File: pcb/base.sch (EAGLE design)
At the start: 2 parts, among them IC1 27C64L

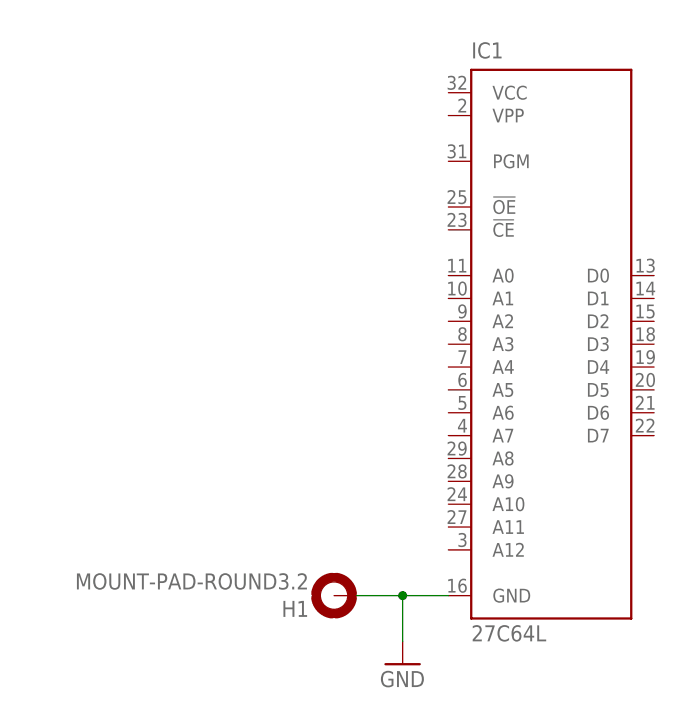
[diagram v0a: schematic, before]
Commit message: Changed mounting pad for the cufflink back.
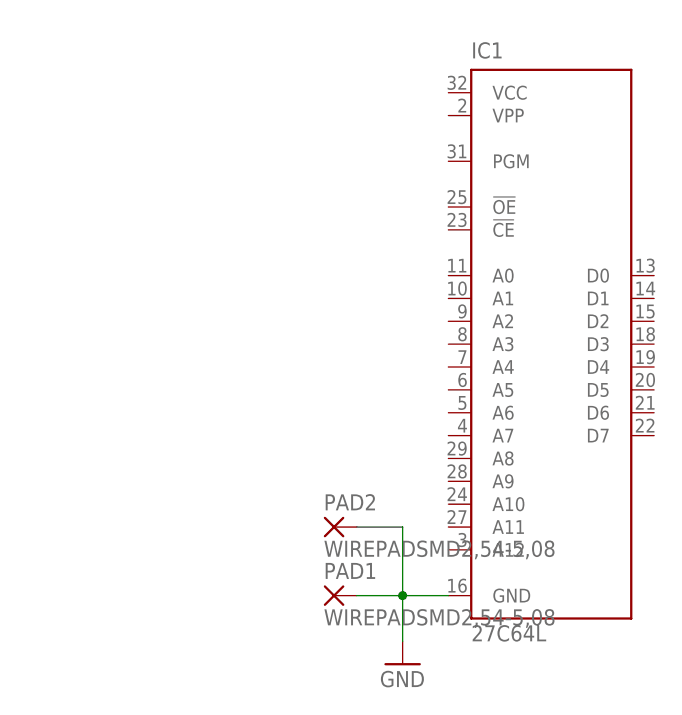
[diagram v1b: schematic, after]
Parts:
- removed H1: MOUNT-PAD-ROUND3.2, holes:MOUNT-PAD-ROUND3.2
- added PAD1, PAD2: WIREPADSMD2,54-5,08, wirepad:WIREPADSMD2,54-5,08
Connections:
- net GND: now also PAD1.P, PAD2.P; no longer H1.MOUNT
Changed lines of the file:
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@@
 <grid distance="0.1" unitdist="inch" unit="inch" style="lines" multiple="1" display="no" altdistance="0.01" altunitdist="inch" altunit="inch"/>
 <layers>
-<layer number="1" name="Top" color="4" fill="1" visible="no" active="no"/>
-<layer number="16" name="Bottom" color="1" fill="1" visible="no" active="no"/>
-<layer number="17" name="Pads" color="2" fill="1" visible="no" active="no"/>
-<layer number="18" name="Vias" color="2" fill="1" visible="no" active="no"/>
-<layer number="19" name="Unrouted" color="6" fill="1" visible="no" active="no"/>
-<layer number="20" name="Dimension" color="15" fill="1" visible="no" active="no"/>
-<layer number="21" name="tPlace" color="7" fill="1" visible="no" active="no"/>
-<layer number="22" name="bPlace" color="7" fill="1" visible="no" active="no"/>
-<layer number="23" name="tOrigins" color="15" fill="1" visible="no" active="no"/>
-<layer number="24" name="bOrigins" color="15" fill="1" visible="no" active="no"/>
-<layer number="25" name="tNames" color="7" fill="1" visible="no" active="no"/>
-<layer number="26" name="bNames" color="7" fill="1" visible="no" active="no"/>
-<layer number="27" name="tValues" color="7" fill="1" visible="no" active="no"/>
-<layer number="28" name="bValues" color="7" fill="1" visible="no" active="no"/>
+<layer number="1" name="Top" color="4" fill="1" visible="yes" active="no"/>
+<layer number="16" name="Bottom" color="1" fill="1" visible="yes" active="no"/>
+<layer number="17" name="Pads" color="2" fill="1" visible="yes" active="no"/>
+<layer number="18" name="Vias" color="2" fill="1" visible="yes" active="no"/>
+<layer number="19" name="Unrouted" color="6" fill="1" visible="yes" active="no"/>
+<layer number="20" name="Dimension" color="15" fill="1" visible="yes" active="no"/>
+<layer number="21" name="tPlace" color="7" fill="1" visible="yes" active="no"/>
+<layer number="22" name="bPlace" color="7" fill="1" visible="yes" active="no"/>
+<layer number="23" name="tOrigins" color="15" fill="1" visible="yes" active="no"/>
+<layer number="24" name="bOrigins" color="15" fill="1" visible="yes" active="no"/>
+<layer number="25" name="tNames" color="7" fill="1" visible="yes" active="no"/>
+<layer number="26" name="bNames" color="7" fill="1" visible="yes" active="no"/>
+<layer number="27" name="tValues" color="7" fill="1" visible="yes" active="no"/>
+<layer number="28" name="bValues" color="7" fill="1" visible="yes" active="no"/>
 <layer number="29" name="tStop" color="7" fill="3" visible="no" active="no"/>
 <layer number="30" name="bStop" color="7" fill="6" visible="no" active="no"/>
@@
 <layer number="35" name="tGlue" color="7" fill="4" visible="no" active="no"/>
 <layer number="36" name="bGlue" color="7" fill="5" visible="no" active="no"/>
-<layer number="37" name="tTest" color="7" fill="1" visible="no" active="no"/>
-<layer number="38" name="bTest" color="7" fill="1" visible="no" active="no"/>
+<layer number="37" name="tTest" color="7" fill="1" visible="yes" active="no"/>
+<layer number="38" name="bTest" color="7" fill="1" visible="yes" active="no"/>
 <layer number="39" name="tKeepout" color="4" fill="11" visible="no" active="no"/>
 <layer number="40" name="bKeepout" color="1" fill="11" visible="no" active="no"/>
@@
 <layer number="44" name="Drills" color="7" fill="1" visible="no" active="no"/>
 <layer number="45" name="Holes" color="7" fill="1" visible="no" active="no"/>
-<layer number="46" name="Milling" color="3" fill="1" visible="no" active="no"/>
-<layer number="47" name="Measures" color="7" fill="1" visible="no" active="no"/>
-<layer number="48" name="Document" color="7" fill="1" visible="no" active="no"/>
-<layer number="49" name="Reference" color="7" fill="1" visible="no" active="no"/>
-<layer number="51" name="tDocu" color="6" fill="1" visible="no" active="no"/>
-<layer number="52" name="bDocu" color="7" fill="1" visible="no" active="no"/>
+<layer number="46" name="Milling" color="3" fill="1" visible="yes" active="no"/>
+<layer number="47" name="Measures" color="7" fill="1" visible="yes" active="no"/>
+<layer number="48" name="Document" color="7" fill="1" visible="yes" active="no"/>
+<layer number="49" name="Reference" color="7" fill="1" visible="yes" active="no"/>
+<layer number="51" name="tDocu" color="7" fill="1" visible="yes" active="no"/>
+<layer number="52" name="bDocu" color="7" fill="1" visible="yes" active="no"/>
 <layer number="90" name="Modules" color="5" fill="1" visible="yes" active="yes"/>
 <layer number="91" name="Nets" color="2" fill="1" visible="yes" active="yes"/>
@@
 <parts>
 <part name="IC1" library="microchip" deviceset="27*64" device="L" technology="C"/>
-<part name="H1" library="holes" deviceset="MOUNT-PAD-ROUND" device="3.2"/>
 <part name="GND1" library="supply1" deviceset="GND" device=""/>
+<part name="PAD1" library="wirepad" deviceset="WIREPAD" device="SMD2,54-5,08" value="WIREPADSMD2,54-5,08"/>
+<part name="PAD2" library="wirepad" deviceset="WIREPAD" device="SMD2,54-5,08" value="WIREPADSMD2,54-5,08"/>
 </parts>
 <sheets>
@@
 <instances>
 <instance part="IC1" gate="G$1" x="15.24" y="38.1"/>
-<instance part="H1" gate="G$1" x="-7.62" y="10.16" rot="R180"/>
 <instance part="GND1" gate="1" x="0" y="2.54"/>
+<instance part="PAD1" gate="G$1" x="-7.62" y="10.16"/>
+<instance part="PAD2" gate="G$1" x="-7.62" y="17.78"/>
 </instances>
 <busses>
@@
 <pinref part="IC1" gate="G$1" pin="GND"/>
 <wire x1="0" y1="10.16" x2="5.08" y2="10.16" width="0.1524" layer="91"/>
-<pinref part="H1" gate="G$1" pin="MOUNT"/>
-<wire x1="0" y1="10.16" x2="-5.08" y2="10.16" width="0.1524" layer="91"/>
+<pinref part="PAD1" gate="G$1" pin="P"/>
+<wire x1="-5.08" y1="10.16" x2="0" y2="10.16" width="0.1524" layer="91"/>
+<wire x1="0" y1="10.16" x2="0" y2="17.78" width="0.1524" layer="91"/>
+<pinref part="PAD2" gate="G$1" pin="P"/>
+<wire x1="0" y1="17.78" x2="-5.08" y2="17.78" width="0.1524" layer="91"/>
 <junction x="0" y="10.16"/>
 </segment>

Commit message: Connected the rest of the pins.
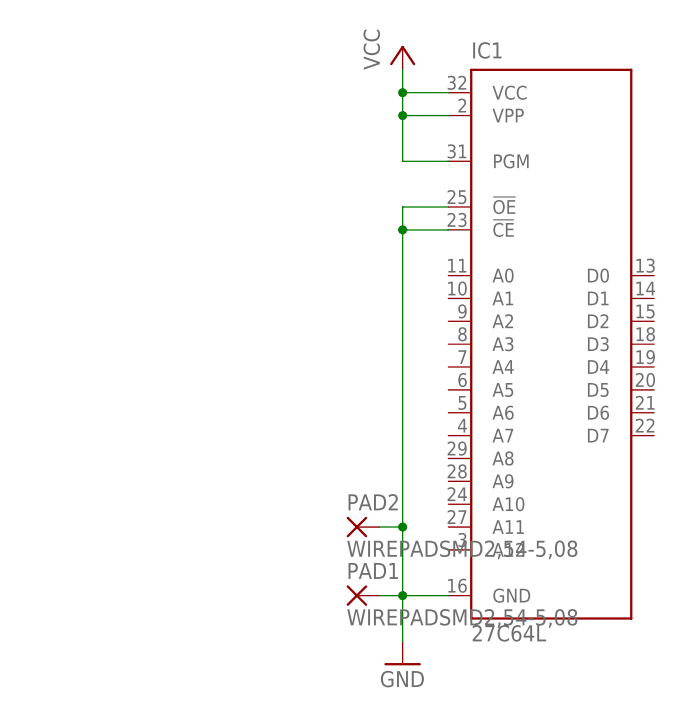
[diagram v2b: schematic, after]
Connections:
- new net VCC: IC1.PGM, IC1.VCC, IC1.VPP
- net GND: now also IC1.!CE, IC1.!OE
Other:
- moved on the sheet: PAD1, PAD2
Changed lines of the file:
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@@
 <grid distance="0.1" unitdist="inch" unit="inch" style="lines" multiple="1" display="no" altdistance="0.01" altunitdist="inch" altunit="inch"/>
 <layers>
-<layer number="1" name="Top" color="4" fill="1" visible="yes" active="no"/>
-<layer number="16" name="Bottom" color="1" fill="1" visible="yes" active="no"/>
-<layer number="17" name="Pads" color="2" fill="1" visible="yes" active="no"/>
-<layer number="18" name="Vias" color="2" fill="1" visible="yes" active="no"/>
-<layer number="19" name="Unrouted" color="6" fill="1" visible="yes" active="no"/>
-<layer number="20" name="Dimension" color="15" fill="1" visible="yes" active="no"/>
-<layer number="21" name="tPlace" color="7" fill="1" visible="yes" active="no"/>
-<layer number="22" name="bPlace" color="7" fill="1" visible="yes" active="no"/>
-<layer number="23" name="tOrigins" color="15" fill="1" visible="yes" active="no"/>
-<layer number="24" name="bOrigins" color="15" fill="1" visible="yes" active="no"/>
-<layer number="25" name="tNames" color="7" fill="1" visible="yes" active="no"/>
-<layer number="26" name="bNames" color="7" fill="1" visible="yes" active="no"/>
-<layer number="27" name="tValues" color="7" fill="1" visible="yes" active="no"/>
-<layer number="28" name="bValues" color="7" fill="1" visible="yes" active="no"/>
+<layer number="1" name="Top" color="4" fill="1" visible="no" active="no"/>
+<layer number="16" name="Bottom" color="1" fill="1" visible="no" active="no"/>
+<layer number="17" name="Pads" color="2" fill="1" visible="no" active="no"/>
+<layer number="18" name="Vias" color="2" fill="1" visible="no" active="no"/>
+<layer number="19" name="Unrouted" color="6" fill="1" visible="no" active="no"/>
+<layer number="20" name="Dimension" color="15" fill="1" visible="no" active="no"/>
+<layer number="21" name="tPlace" color="7" fill="1" visible="no" active="no"/>
+<layer number="22" name="bPlace" color="7" fill="1" visible="no" active="no"/>
+<layer number="23" name="tOrigins" color="15" fill="1" visible="no" active="no"/>
+<layer number="24" name="bOrigins" color="15" fill="1" visible="no" active="no"/>
+<layer number="25" name="tNames" color="7" fill="1" visible="no" active="no"/>
+<layer number="26" name="bNames" color="7" fill="1" visible="no" active="no"/>
+<layer number="27" name="tValues" color="7" fill="1" visible="no" active="no"/>
+<layer number="28" name="bValues" color="7" fill="1" visible="no" active="no"/>
 <layer number="29" name="tStop" color="7" fill="3" visible="no" active="no"/>
 <layer number="30" name="bStop" color="7" fill="6" visible="no" active="no"/>
@@
 <layer number="35" name="tGlue" color="7" fill="4" visible="no" active="no"/>
 <layer number="36" name="bGlue" color="7" fill="5" visible="no" active="no"/>
-<layer number="37" name="tTest" color="7" fill="1" visible="yes" active="no"/>
-<layer number="38" name="bTest" color="7" fill="1" visible="yes" active="no"/>
+<layer number="37" name="tTest" color="7" fill="1" visible="no" active="no"/>
+<layer number="38" name="bTest" color="7" fill="1" visible="no" active="no"/>
 <layer number="39" name="tKeepout" color="4" fill="11" visible="no" active="no"/>
 <layer number="40" name="bKeepout" color="1" fill="11" visible="no" active="no"/>
@@
 <layer number="44" name="Drills" color="7" fill="1" visible="no" active="no"/>
 <layer number="45" name="Holes" color="7" fill="1" visible="no" active="no"/>
-<layer number="46" name="Milling" color="3" fill="1" visible="yes" active="no"/>
-<layer number="47" name="Measures" color="7" fill="1" visible="yes" active="no"/>
-<layer number="48" name="Document" color="7" fill="1" visible="yes" active="no"/>
-<layer number="49" name="Reference" color="7" fill="1" visible="yes" active="no"/>
-<layer number="51" name="tDocu" color="7" fill="1" visible="yes" active="no"/>
-<layer number="52" name="bDocu" color="7" fill="1" visible="yes" active="no"/>
+<layer number="46" name="Milling" color="3" fill="1" visible="no" active="no"/>
+<layer number="47" name="Measures" color="7" fill="1" visible="no" active="no"/>
+<layer number="48" name="Document" color="7" fill="1" visible="no" active="no"/>
+<layer number="49" name="Reference" color="7" fill="1" visible="no" active="no"/>
+<layer number="51" name="tDocu" color="7" fill="1" visible="no" active="no"/>
+<layer number="52" name="bDocu" color="7" fill="1" visible="no" active="no"/>
 <layer number="90" name="Modules" color="5" fill="1" visible="yes" active="yes"/>
 <layer number="91" name="Nets" color="2" fill="1" visible="yes" active="yes"/>
@@
 <part name="PAD1" library="wirepad" deviceset="WIREPAD" device="SMD2,54-5,08" value="WIREPADSMD2,54-5,08"/>
 <part name="PAD2" library="wirepad" deviceset="WIREPAD" device="SMD2,54-5,08" value="WIREPADSMD2,54-5,08"/>
+<part name="P+1" library="supply1" deviceset="VCC" device=""/>
 </parts>
 <sheets>
@@
 <instance part="IC1" gate="G$1" x="15.24" y="38.1"/>
 <instance part="GND1" gate="1" x="0" y="2.54"/>
-<instance part="PAD1" gate="G$1" x="-7.62" y="10.16"/>
-<instance part="PAD2" gate="G$1" x="-7.62" y="17.78"/>
+<instance part="PAD1" gate="G$1" x="-5.08" y="10.16"/>
+<instance part="PAD2" gate="G$1" x="-5.08" y="17.78"/>
+<instance part="P+1" gate="VCC" x="0" y="71.12"/>
 </instances>
 <busses>
@@
 <wire x1="0" y1="10.16" x2="5.08" y2="10.16" width="0.1524" layer="91"/>
 <pinref part="PAD1" gate="G$1" pin="P"/>
-<wire x1="-5.08" y1="10.16" x2="0" y2="10.16" width="0.1524" layer="91"/>
+<wire x1="-2.54" y1="10.16" x2="0" y2="10.16" width="0.1524" layer="91"/>
 <wire x1="0" y1="10.16" x2="0" y2="17.78" width="0.1524" layer="91"/>
 <pinref part="PAD2" gate="G$1" pin="P"/>
-<wire x1="0" y1="17.78" x2="-5.08" y2="17.78" width="0.1524" layer="91"/>
+<wire x1="0" y1="17.78" x2="-2.54" y2="17.78" width="0.1524" layer="91"/>
 <junction x="0" y="10.16"/>
+<pinref part="IC1" gate="G$1" pin="!OE"/>
+<wire x1="0" y1="53.34" x2="0" y2="50.8" width="0.1524" layer="91"/>
+<wire x1="0" y1="50.8" x2="0" y2="17.78" width="0.1524" layer="91"/>
+<wire x1="5.08" y1="53.34" x2="0" y2="53.34" width="0.1524" layer="91"/>
+<pinref part="IC1" gate="G$1" pin="!CE"/>
+<wire x1="5.08" y1="50.8" x2="0" y2="50.8" width="0.1524" layer="91"/>
+<junction x="0" y="50.8"/>
+<junction x="0" y="17.78"/>
+</segment>
+</net>
+<net name="VCC" class="0">
+<segment>
+<pinref part="IC1" gate="G$1" pin="VCC"/>
+<pinref part="P+1" gate="VCC" pin="VCC"/>
+<wire x1="5.08" y1="66.04" x2="0" y2="66.04" width="0.1524" layer="91"/>
+<wire x1="0" y1="66.04" x2="0" y2="68.58" width="0.1524" layer="91"/>
+<pinref part="IC1" gate="G$1" pin="VPP"/>
+<wire x1="5.08" y1="63.5" x2="0" y2="63.5" width="0.1524" layer="91"/>
+<wire x1="0" y1="63.5" x2="0" y2="66.04" width="0.1524" layer="91"/>
+<junction x="0" y="66.04"/>
+<pinref part="IC1" gate="G$1" pin="PGM"/>
+<wire x1="5.08" y1="58.42" x2="0" y2="58.42" width="0.1524" layer="91"/>
+<wire x1="0" y1="58.42" x2="0" y2="63.5" width="0.1524" layer="91"/>
+<junction x="0" y="63.5"/>
 </segment>
 </net>
@@
 </sheet>
 </sheets>
+<errors>
+</errors>
 </schematic>
 </drawing>
